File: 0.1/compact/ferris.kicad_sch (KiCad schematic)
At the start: 95 parts, among them J1 USB C, K0_0 KEYSW, K0_1 KEYSW, K0_2 KEYSW, K0_3 KEYSW, K0_4 KEYSW, K0_5 KEYSW, K0_6 KEYSW, K0_7 KEYSW, K0_8 KEYSW, K0_9 KEYSW, K1_0 KEYSW, K1_1 KEYSW, K1_2 KEYSW, K1_3 KEYSW, K1_4 KEYSW, K1_5 KEYSW, K1_6 KEYSW, K1_7 KEYSW, K1_8 KEYSW, K1_9 KEYSW, K2_0 KEYSW, K2_1 KEYSW, K2_2 KEYSW, K2_3 KEYSW, K2_4 KEYSW, K2_5 KEYSW, K2_6 KEYSW, K2_7 KEYSW, K2_8 KEYSW, K2_9 KEYSW, K3_3 KEYSW, K3_4 KEYSW, K3_5 KEYSW, K3_6 KEYSW, SW1 SW_PUSH, U1 ATmega32U4-AU, U2 MCP23017_SO, Y1 Crystal

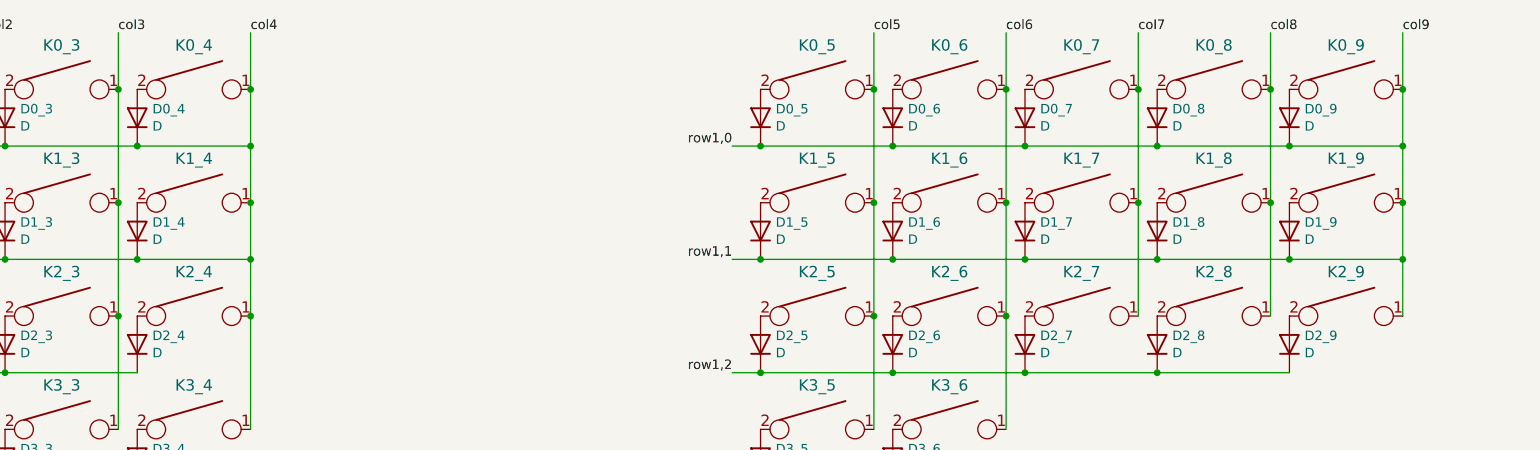
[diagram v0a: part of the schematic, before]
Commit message: Again, fix schematic bug connecting rows directly to rightmost column
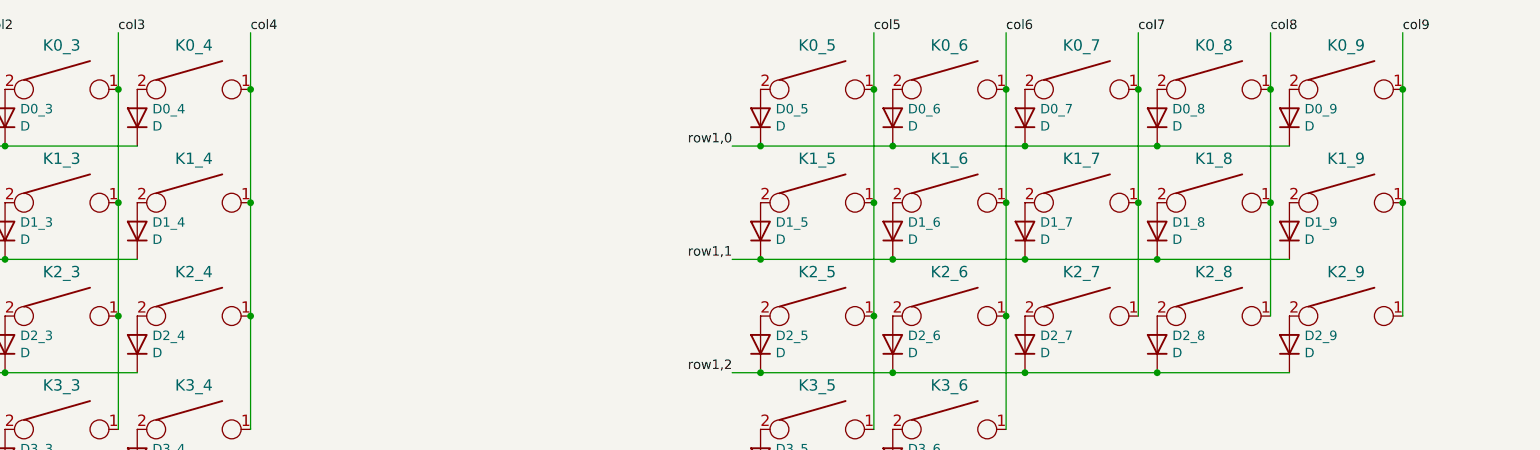
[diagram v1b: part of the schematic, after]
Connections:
- net col4: no longer D0_0.1 (K), D0_1.1 (K), D0_2.1 (K), D0_3.1 (K), D0_4.1 (K), D1_0.1 (K), D1_1.1 (K), D1_2.1 (K), D1_3.1 (K), D1_4.1 (K), U1.10 (PB2), U1.11 (PB3)
- net col9: no longer D0_5.1 (K), D0_6.1 (K), D0_7.1 (K), D0_8.1 (K), D0_9.1 (K), D1_5.1 (K), D1_6.1 (K), D1_7.1 (K), D1_8.1 (K), D1_9.1 (K), U2.1 (GPB0), U2.2 (GPB1)
- new net row0,0: D0_0.1 (K), D0_1.1 (K), D0_2.1 (K), D0_3.1 (K), D0_4.1 (K), U1.11 (PB3)
- new net row0,1: D1_0.1 (K), D1_1.1 (K), D1_2.1 (K), D1_3.1 (K), D1_4.1 (K), U1.10 (PB2)
- new net row1,0: D0_5.1 (K), D0_6.1 (K), D0_7.1 (K), D0_8.1 (K), D0_9.1 (K), U2.1 (GPB0)
- new net row1,1: D1_5.1 (K), D1_6.1 (K), D1_7.1 (K), D1_8.1 (K), D1_9.1 (K), U2.2 (GPB1)
